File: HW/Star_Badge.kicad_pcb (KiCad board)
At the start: 2 copper layers, 180 x 171.6 mm, 55 parts, among them J1 AVR-ISP-6, J2 10118194-0001LF, Q1 Q_NMOS_DGS, Q2 Q_PMOS_DGS, U1 ATTINY861-15XD, U2 TPS613221ADBVT, U3 AP7363-33D-13, X1 Badgelife_sao_connector_v169b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, X2 Badgelife_sao_connector_v169b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, X3 Badgelife_sao_connector_v169b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

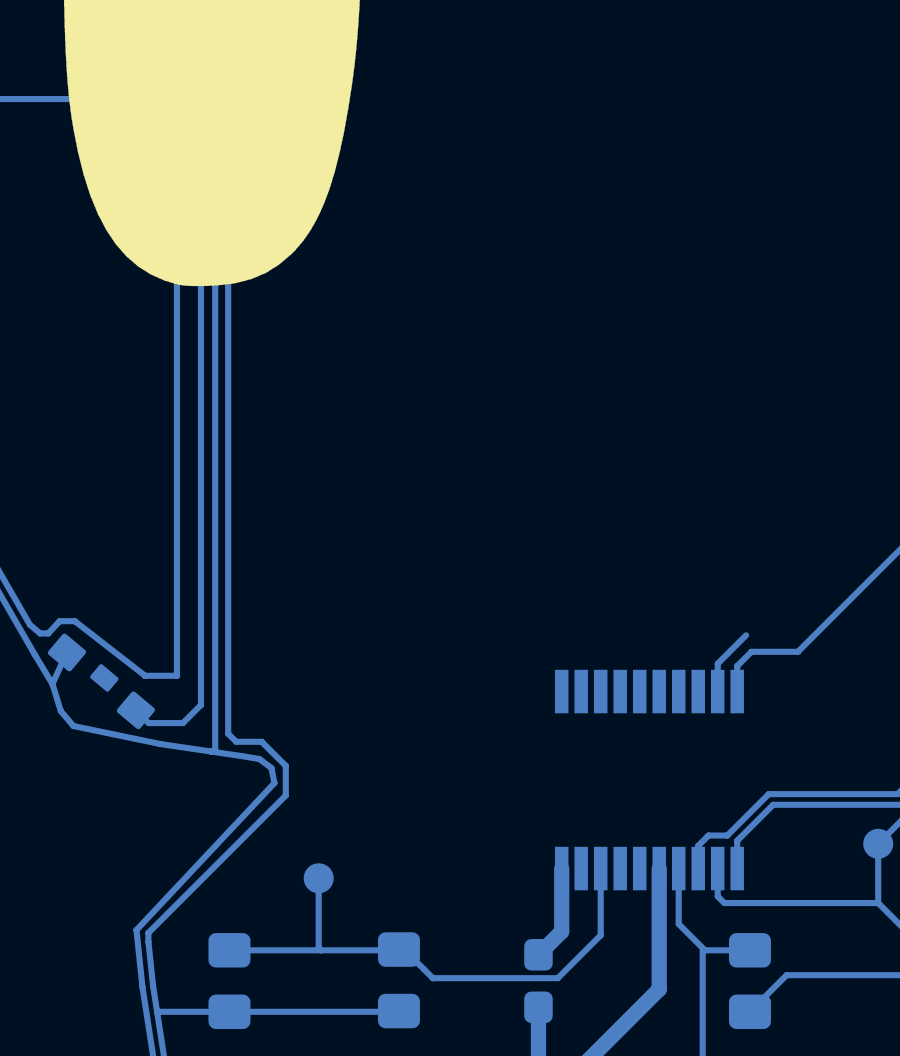
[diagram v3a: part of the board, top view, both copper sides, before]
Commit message: changed the enable pins for better routing and labled the associated star.
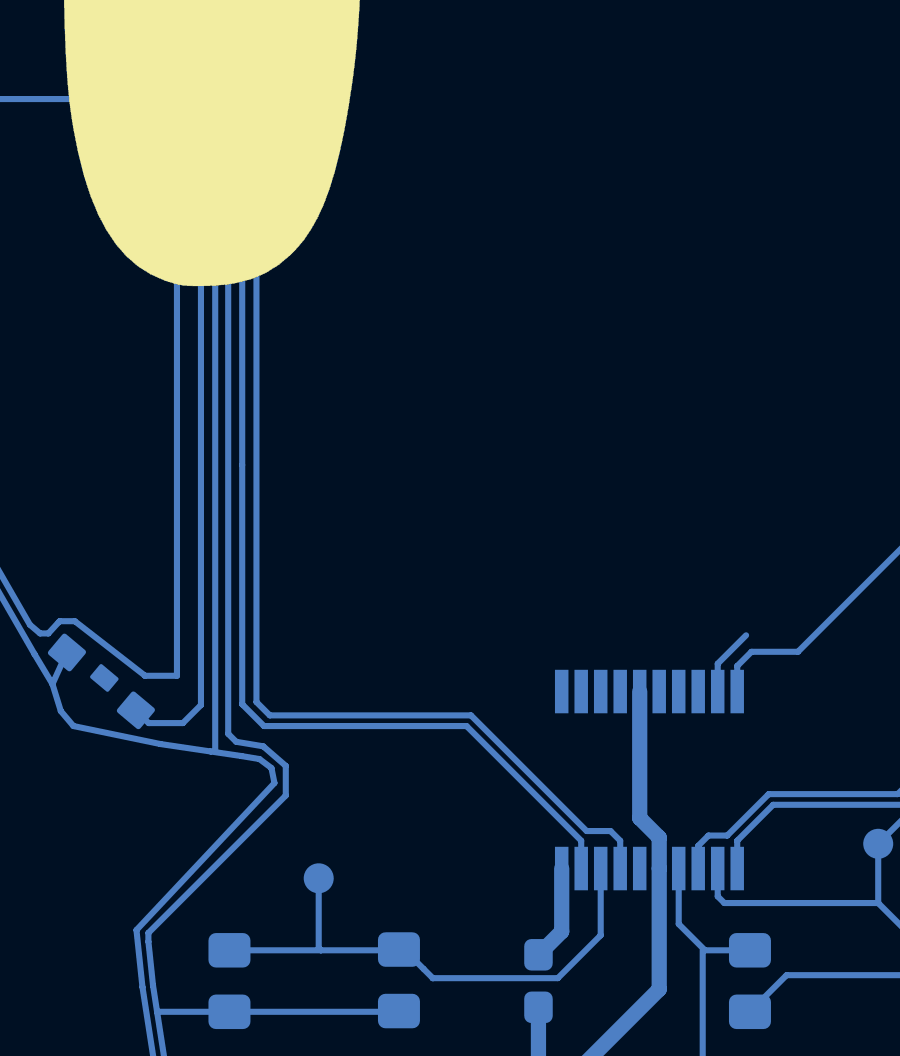
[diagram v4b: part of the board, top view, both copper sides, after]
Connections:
- D1 pad 1: /EN_RGB0 -> /EN_RGB2
- D10 pad 1: /EN_RGB3 -> /EN_RGB0
- D11 pad 1: /EN_RGB3 -> /EN_RGB0
- D12 pad 1: /EN_RGB3 -> /EN_RGB0
- D13 pad 1: /EN_RGB4 -> /EN_RGB1
- D14 pad 1: /EN_RGB4 -> /EN_RGB1
- D15 pad 1: /EN_RGB4 -> /EN_RGB1
- D2 pad 1: /EN_RGB0 -> /EN_RGB2
- D3 pad 1: /EN_RGB0 -> /EN_RGB2
- D4 pad 1: /EN_RGB1 -> /EN_RGB3
- D5 pad 1: /EN_RGB1 -> /EN_RGB3
- D6 pad 1: /EN_RGB1 -> /EN_RGB3
- D7 pad 1: /EN_RGB2 -> /EN_RGB4
- D8 pad 1: /EN_RGB2 -> /EN_RGB4
- D9 pad 1: /EN_RGB2 -> /EN_RGB4
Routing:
- net /GPIO_2_2: track 0.00 -> 32.0 mm
- net /Button: track 29.6 -> 61.1 mm
- net /EN_RGB1: track 56.3 -> 66.7 mm
- net /EN_RGB2: track 62.6 -> 55.5 mm
- net /VBUS: track 237.4 -> 243.5 mm
- net /EN_RGB0: track 55.5 -> 60.7 mm
- net /EN_RGB3: track 60.7 -> 56.3 mm
- net /EN_RGB4: track 66.7 -> 62.6 mm

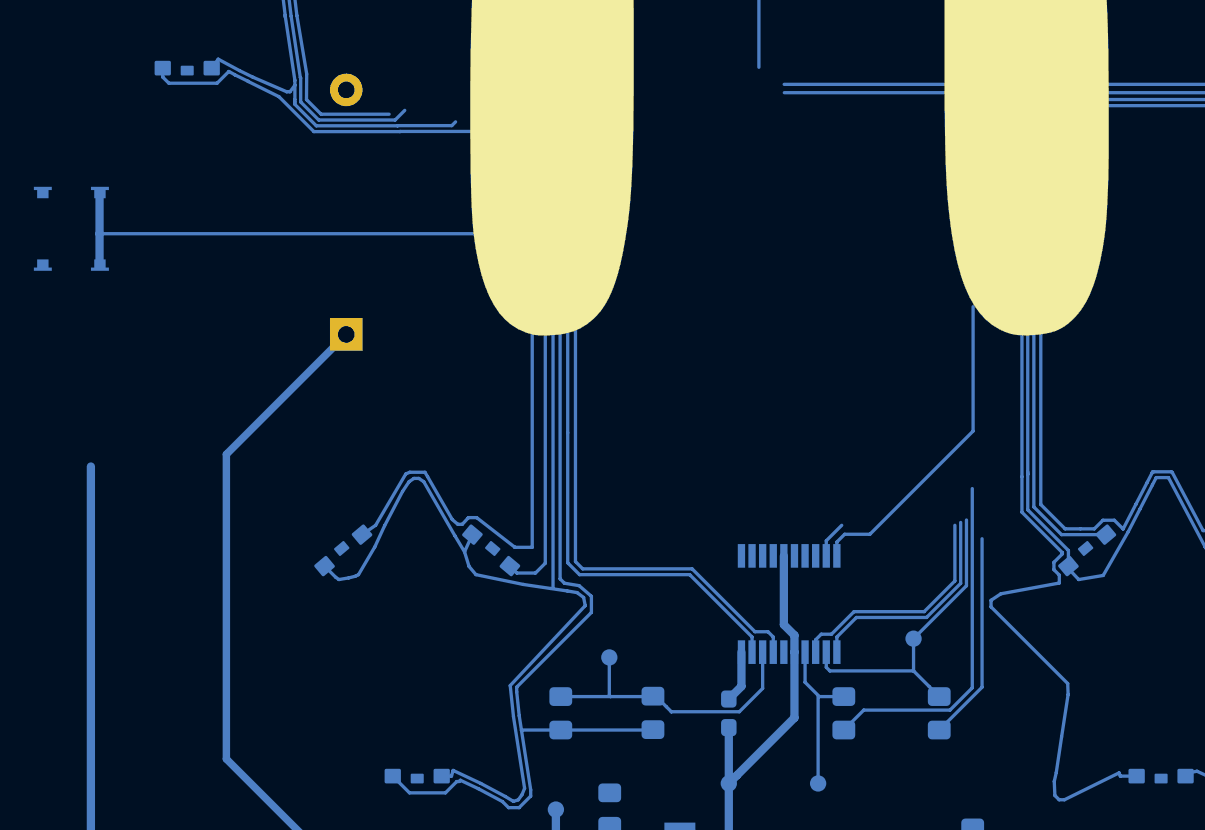
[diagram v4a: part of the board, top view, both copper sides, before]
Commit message: spaced out the traces on Stars 3 and 4. Connect button
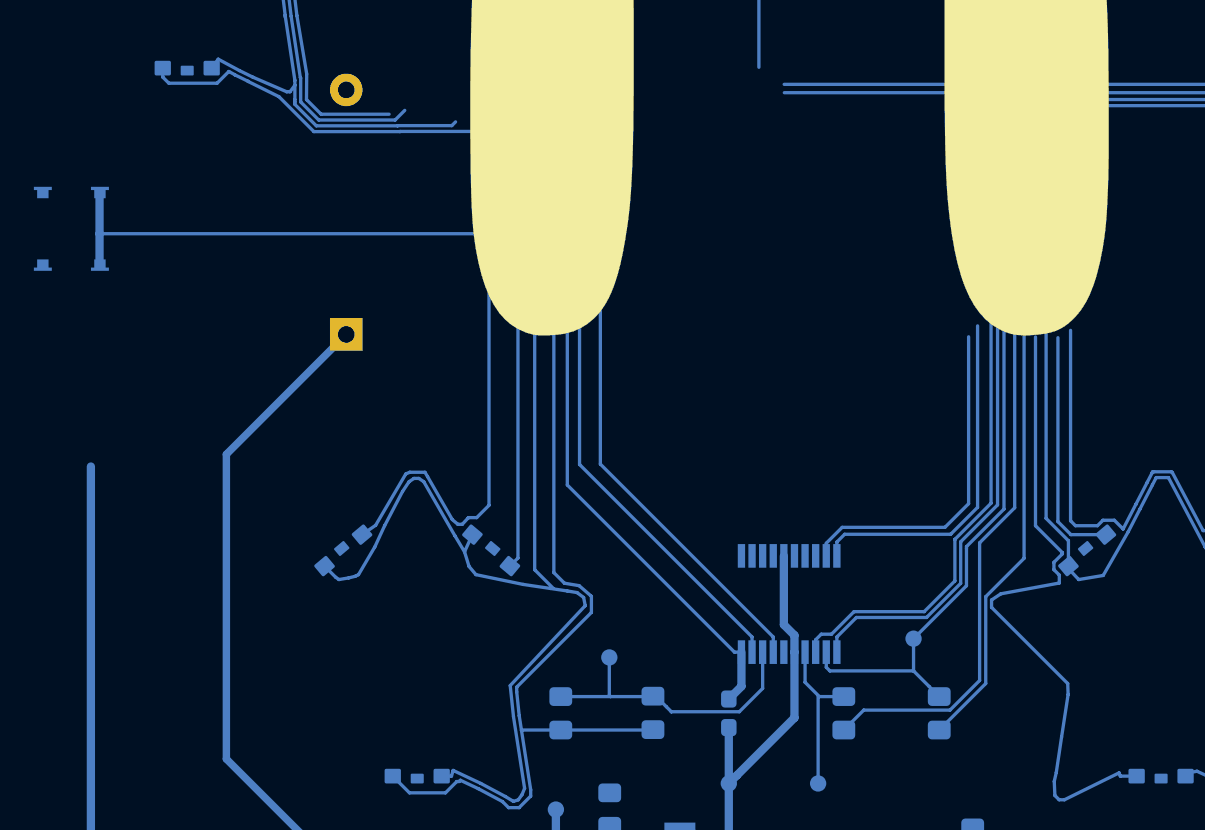
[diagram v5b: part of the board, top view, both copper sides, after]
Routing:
- net /~RESET: track 3.20 -> 32.9 mm
- net /GPIO_1_2: track 2.27 -> 20.7 mm
- net /SCL_SCK: track 14.2 -> 28.5 mm
- net /SDA_MOSI: track 13.6 -> 27.2 mm
- net /R_PWM__MISO: track 19.2 -> 32.7 mm
- net /R_LED_BUS: track 196.8 -> 207.1 mm
- net /EN_RGB1: track 66.7 -> 74.4 mm
- net /G_LED_BUS: track 221.7 -> 228.8 mm
- net /B_LED_BUS: track 143.2 -> 149.3 mm
- net /GPIO_2_2: track 32.0 -> 27.1 mm
- net /Button: track 61.1 -> 63.7 mm, vias 0 -> 2
- net /GPIO_1_1: track 19.6 -> 21.5 mm
- net /EN_RGB0: track 60.7 -> 58.9 mm
- net /EN_RGB4: track 62.6 -> 61.9 mm
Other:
- rule via_min_drill: 0.2 -> 0.3

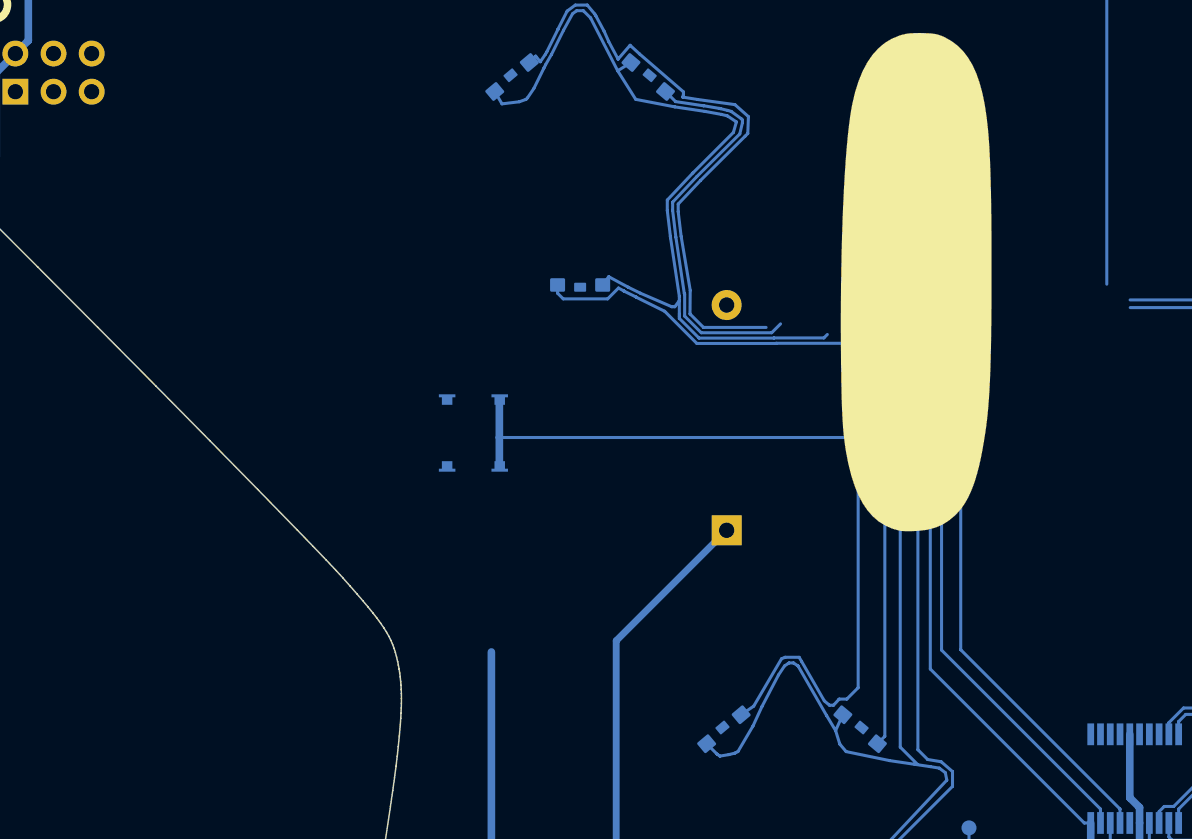
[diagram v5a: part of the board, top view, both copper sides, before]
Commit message: star 5 wired
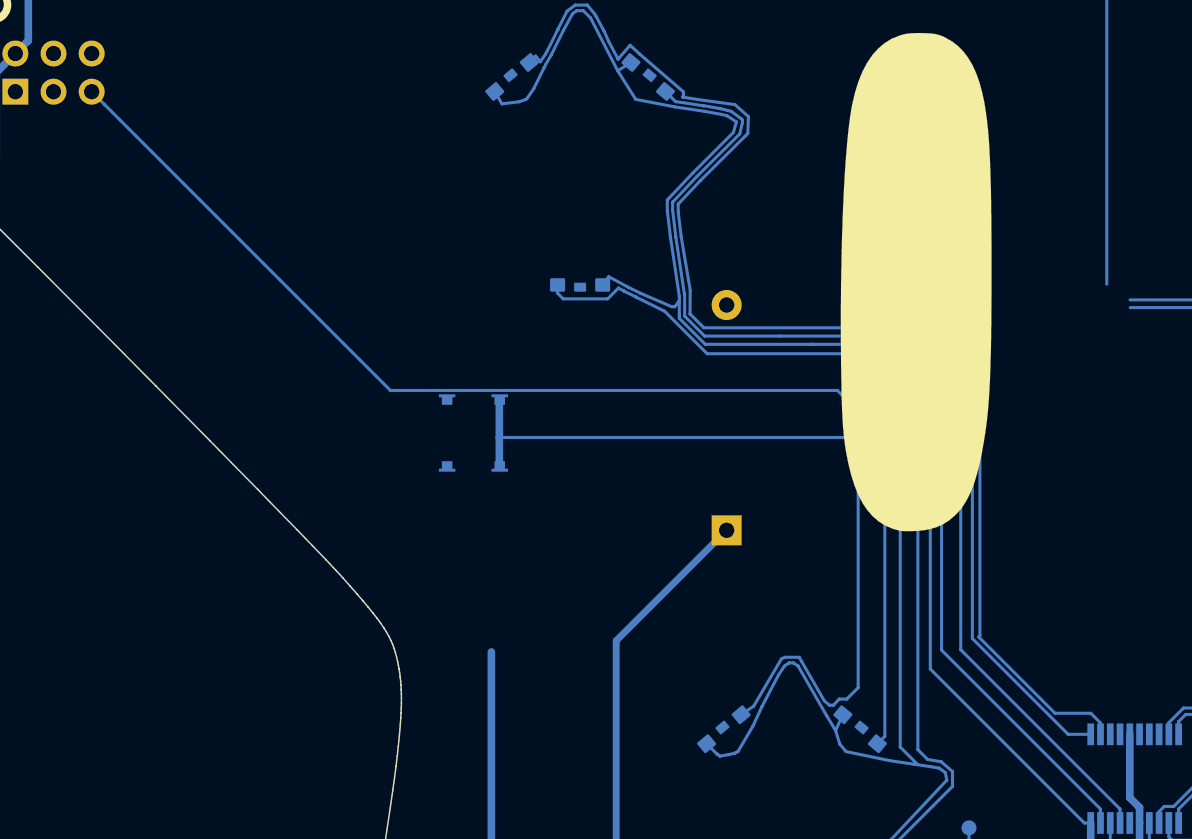
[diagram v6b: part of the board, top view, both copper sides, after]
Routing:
- net /GPIO_2_2: track 27.1 -> 98.0 mm, vias 0 -> 2
- net /EN_RGB3: track 56.3 -> 94.6 mm
- net /EN_RGB4: track 61.9 -> 97.1 mm, vias 0 -> 2
- net /R_LED_BUS: track 207.1 -> 225.7 mm, vias 0 -> 2
- net /G_LED_BUS: track 228.8 -> 243.0 mm, vias 0 -> 2
- net /B_LED_BUS: track 149.3 -> 161.0 mm

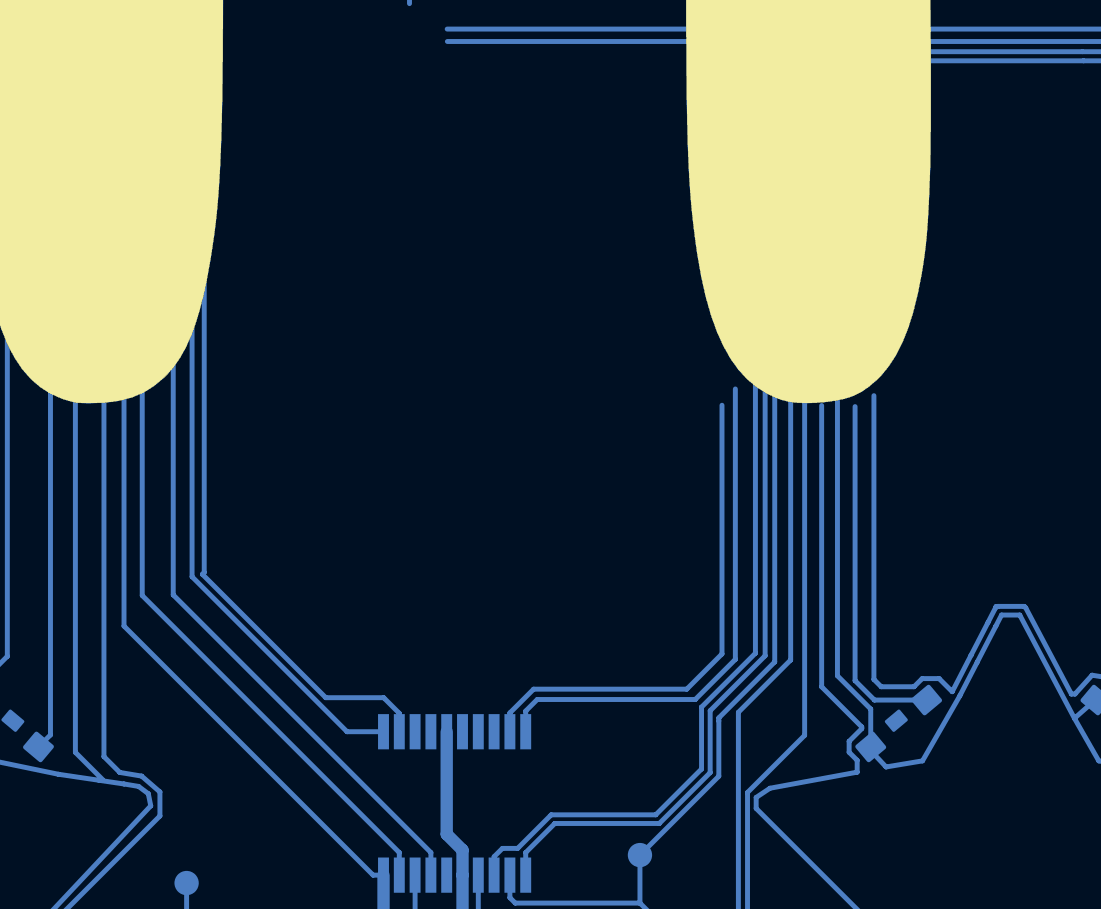
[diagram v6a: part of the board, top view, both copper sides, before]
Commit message: 43 unrouted singlas
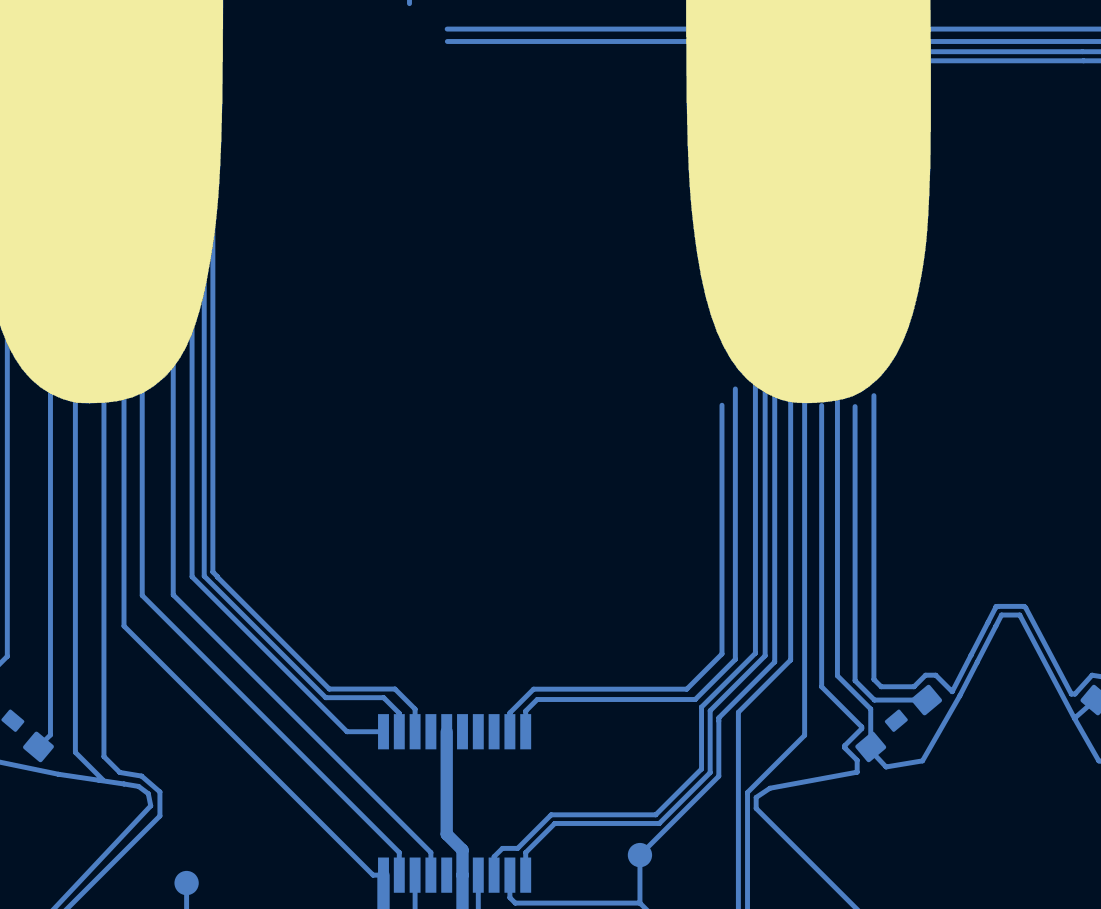
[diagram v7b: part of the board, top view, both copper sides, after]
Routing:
- net /EN_RGB2: track 55.5 -> 85.6 mm

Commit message: Star 2 and 3 routing
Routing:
- net /GPIO_2_1: track 0.00 -> 21.2 mm
- net /EN_RGB0: track 58.9 -> 67.3 mm
- net /EN_RGB1: track 74.4 -> 66.3 mm
- net /B_LED_BUS: track 161.1 -> 168.1 mm, vias 0 -> 2
- net /G_LED_BUS: track 243.0 -> 238.3 mm, vias 2 -> 4
- net /R_LED_BUS: track 225.8 -> 224.0 mm, vias 2 -> 6
